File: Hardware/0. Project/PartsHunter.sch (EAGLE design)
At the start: 54 parts, among them CN1 2.1MMJACKTHM, IC1 PCF8574P, IC2 LM1117-3.3, Q1 16 MHz, U1 ATMEGA328P-AU

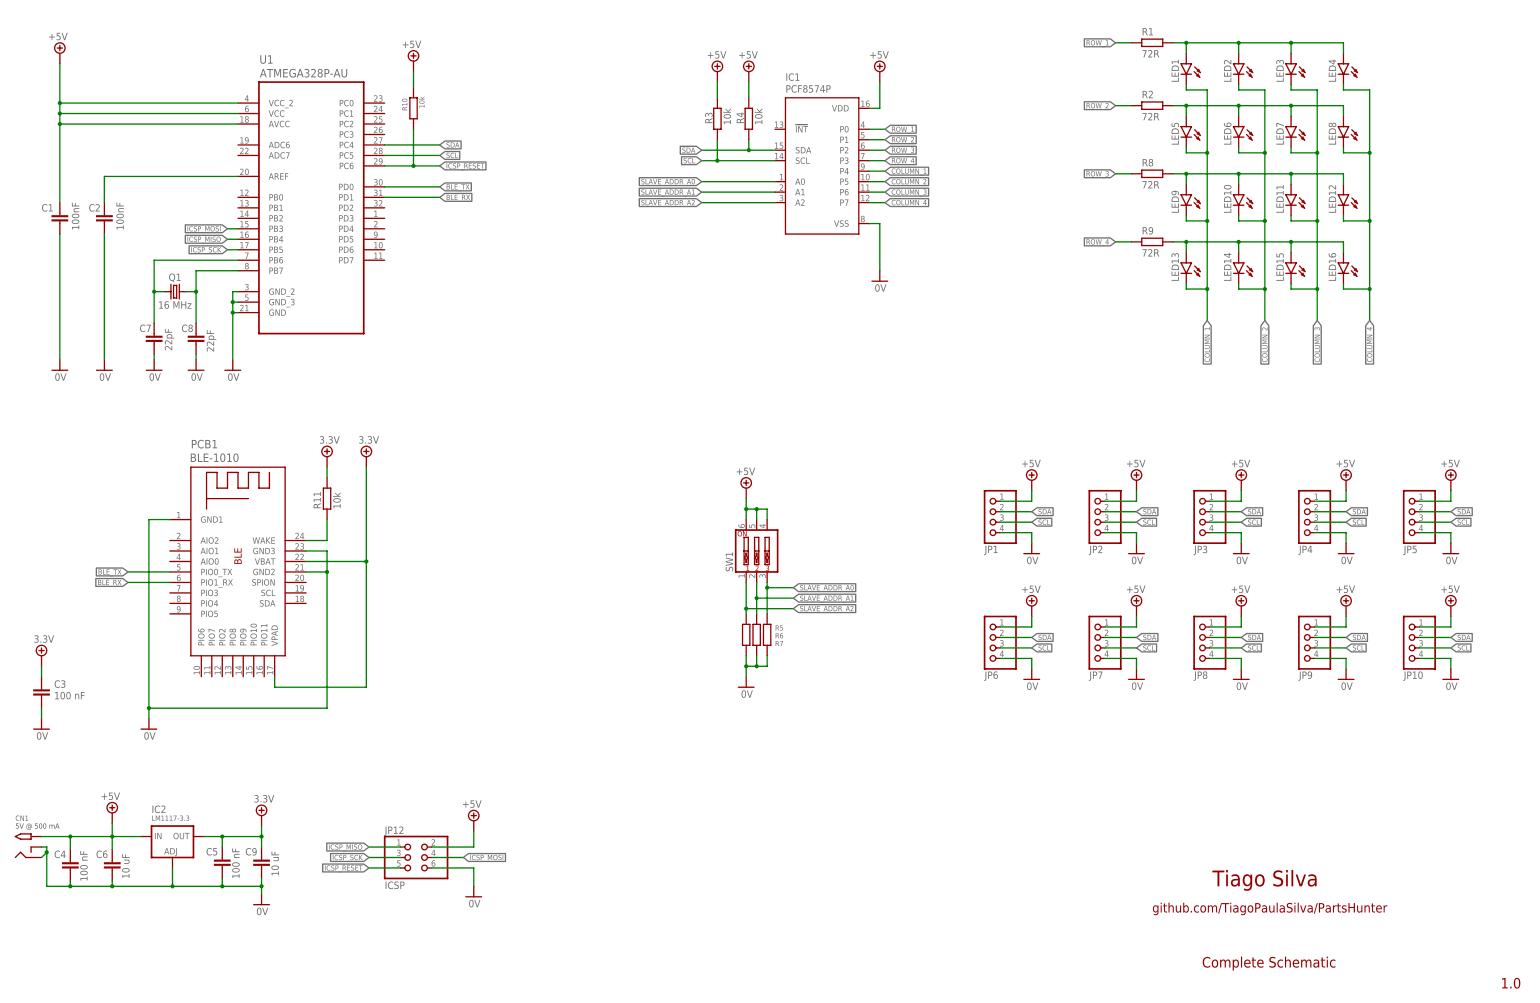
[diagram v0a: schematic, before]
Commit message: I2C pull-ups moved to master's circuit area
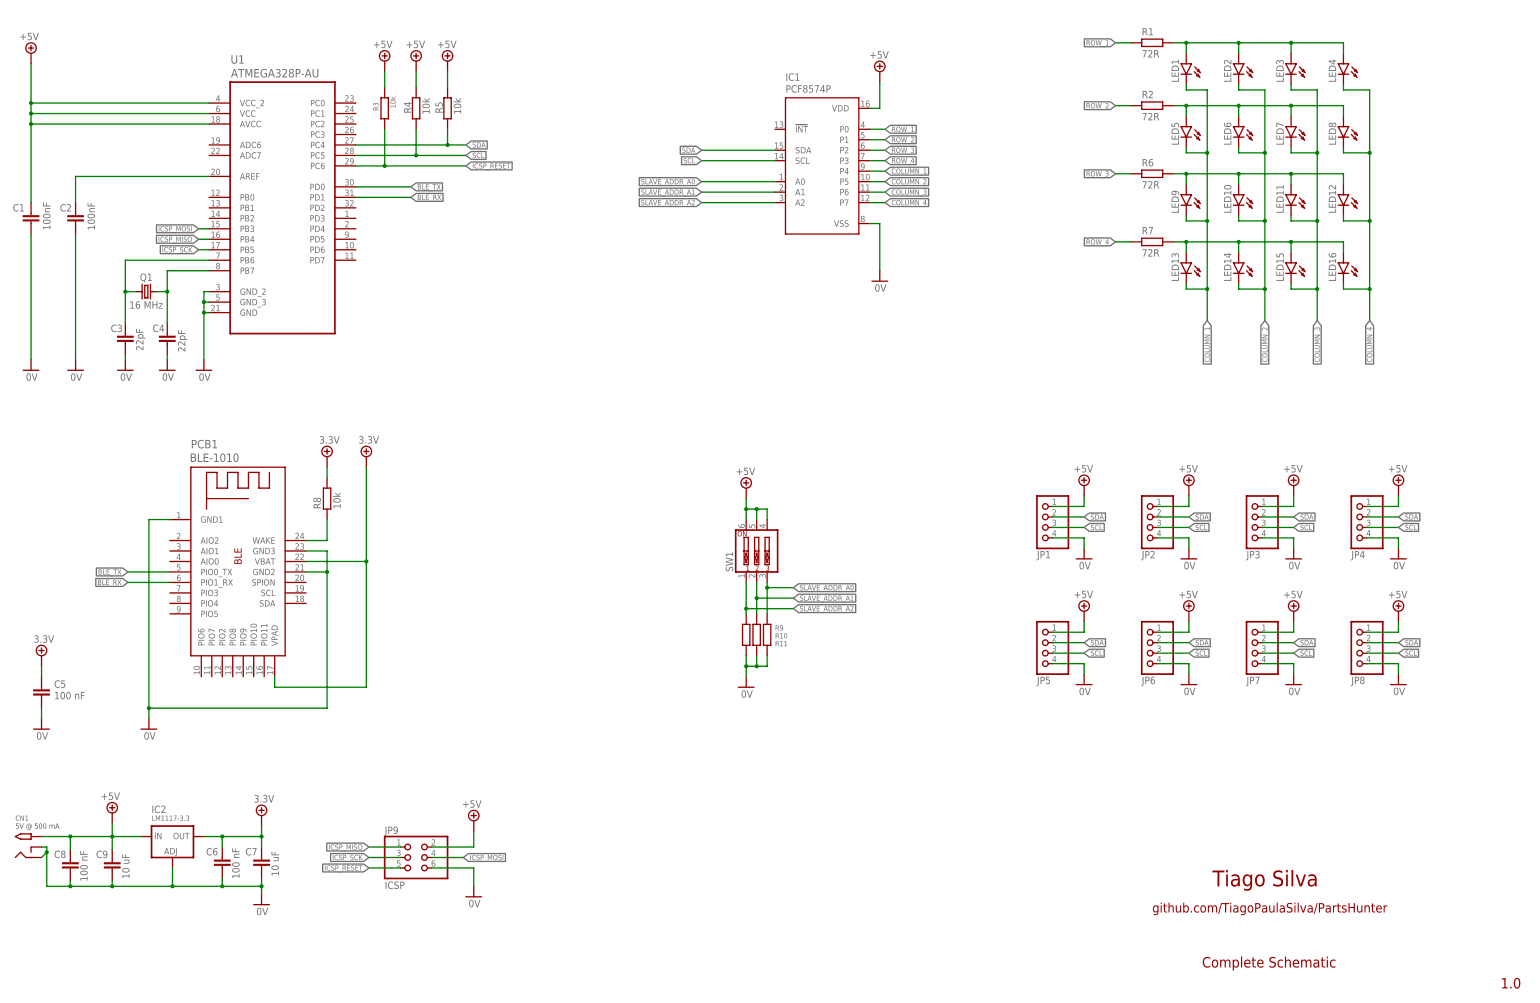
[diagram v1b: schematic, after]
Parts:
- removed JP10: (no value), pinhead:PINHD-1X4
- removed JP12: ICSP, pinhead:PINHD-2X3
- C3, C4: value 100 nF -> 22pF
- C6: value 10 uF -> 100 nF
- C7: value 22pF -> 10 uF
- C8: value 22pF -> 100 nF
- JP5: device pinhead:PINHD-1X4 -> pinhead:PINHD-1X4/90
- JP9: value (none) -> ICSP; device pinhead:PINHD-1X4/90 -> pinhead:PINHD-2X3
- R11: device rcl:R-EU_R0603 -> rcl:R-EU_R0805
- R6, R7: value 10k -> 72R
- R8: value 72R -> 10k; device rcl:R-EU_R0805 -> rcl:R-EU_R0603
- R9: value 72R -> 10k
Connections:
- net +5V: now also C8.1, C9.1, JP9.2, R5.1; no longer C4.1, C6.1, JP10.1, JP12.2, JP9.1, R10.1
- net 0V: now also C3.1, C4.1, C7.2, C8.2, JP9.6, R10.2, R11.2, R9.2; no longer C3.2, C4.2, C7.1, C8.1, JP10.4, JP12.6, JP9.4, R5.2, R6.2, R7.2
- net 3.3V: now also C6.1, C7.1, R8.1; no longer C3.1, C9.1, R11.1
- net BLE_WAKE: now also R8.2; no longer R11.2
- net ICSP_MISO: now also JP9.1; no longer JP12.1
- net ICSP_MOSI: now also JP9.4; no longer JP12.4
- net ICSP_RESET: now also JP9.5, R3.2; no longer JP12.5, R10.2
- net ICSP_SCK: now also JP9.3; no longer JP12.3
- net N$1: now also C3.2; no longer C7.2
- net N$2: now also C4.2; no longer C8.2
- net N$7: now also R6.1; no longer R8.1
- net N$8: now also R7.1; no longer R9.1
- net ROW_3: now also R6.2; no longer R8.2
- net ROW_4: now also R7.2; no longer R9.2
- net SCL: now also R4.2; no longer JP10.3, JP9.3, R3.2
- net SDA: now also R5.2; no longer JP10.2, JP9.2, R4.2
- net SLAVE_ADDR_A0: now also R11.1; no longer R7.1
- net SLAVE_ADDR_A1: now also R10.1; no longer R6.1
- net SLAVE_ADDR_A2: now also R9.1; no longer R5.1
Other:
- moved on the sheet: C1, C2, C3, C4, C5, C6, C7, C8, C9, JP1, JP2, JP3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

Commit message: SMD and PTH led option added
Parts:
- LED1, LED10, LED11, LED12, LED13, LED14, LED15, LED16, LED2, LED3, LED4, LED5, LED6, LED7, LED8, LED9: device led:LEDKA-3528ASYC -> led2:LEDKA-3528ASYC
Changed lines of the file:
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@@
 <parts>
 <part name="IC1" library="micro-philips" library_urn="urn:adsk.eagle:library:290" deviceset="PCF8574" device="P" package3d_urn="urn:adsk.eagle:package:20171/1"/>
-<part name="LED4" library="led" library_urn="urn:adsk.eagle:library:259" deviceset="LED" device="KA-3528ASYC" package3d_urn="urn:adsk.eagle:package:15831/1"/>
-<part name="LED3" library="led" library_urn="urn:adsk.eagle:library:259" deviceset="LED" device="KA-3528ASYC" package3d_urn="urn:adsk.eagle:package:15831/1"/>
-<part name="LED2" library="led" library_urn="urn:adsk.eagle:library:259" deviceset="LED" device="KA-3528ASYC" package3d_urn="urn:adsk.eagle:package:15831/1"/>
-<part name="LED1" library="led" library_urn="urn:adsk.eagle:library:259" deviceset="LED" device="KA-3528ASYC" package3d_urn="urn:adsk.eagle:package:15831/1"/>
-<part name="LED8" library="led" library_urn="urn:adsk.eagle:library:259" deviceset="LED" device="KA-3528ASYC" package3d_urn="urn:adsk.eagle:package:15831/1"/>
-<part name="LED7" library="led" library_urn="urn:adsk.eagle:library:259" deviceset="LED" device="KA-3528ASYC" package3d_urn="urn:adsk.eagle:package:15831/1"/>
-<part name="LED6" library="led" library_urn="urn:adsk.eagle:library:259" deviceset="LED" device="KA-3528ASYC" package3d_urn="urn:adsk.eagle:package:15831/1"/>
-<part name="LED5" library="led" library_urn="urn:adsk.eagle:library:259" deviceset="LED" device="KA-3528ASYC" package3d_urn="urn:adsk.eagle:package:15831/1"/>
-<part name="LED12" library="led" library_urn="urn:adsk.eagle:library:259" deviceset="LED" device="KA-3528ASYC" package3d_urn="urn:adsk.eagle:package:15831/1"/>
-<part name="LED11" library="led" library_urn="urn:adsk.eagle:library:259" deviceset="LED" device="KA-3528ASYC" package3d_urn="urn:adsk.eagle:package:15831/1"/>
-<part name="LED10" library="led" library_urn="urn:adsk.eagle:library:259" deviceset="LED" device="KA-3528ASYC" package3d_urn="urn:adsk.eagle:package:15831/1"/>
-<part name="LED9" library="led" library_urn="urn:adsk.eagle:library:259" deviceset="LED" device="KA-3528ASYC" package3d_urn="urn:adsk.eagle:package:15831/1"/>
-<part name="LED16" library="led" library_urn="urn:adsk.eagle:library:259" deviceset="LED" device="KA-3528ASYC" package3d_urn="urn:adsk.eagle:package:15831/1"/>
-<part name="LED15" library="led" library_urn="urn:adsk.eagle:library:259" deviceset="LED" device="KA-3528ASYC" package3d_urn="urn:adsk.eagle:package:15831/1"/>
-<part name="LED14" library="led" library_urn="urn:adsk.eagle:library:259" deviceset="LED" device="KA-3528ASYC" package3d_urn="urn:adsk.eagle:package:15831/1"/>
-<part name="LED13" library="led" library_urn="urn:adsk.eagle:library:259" deviceset="LED" device="KA-3528ASYC" package3d_urn="urn:adsk.eagle:package:15831/1"/>
+<part name="LED4" library="led2" deviceset="LED" device="KA-3528ASYC" package3d_urn="urn:adsk.eagle:package:15831/1"/>
+<part name="LED3" library="led2" deviceset="LED" device="KA-3528ASYC" package3d_urn="urn:adsk.eagle:package:15831/1"/>
+<part name="LED2" library="led2" deviceset="LED" device="KA-3528ASYC" package3d_urn="urn:adsk.eagle:package:15831/1"/>
+<part name="LED1" library="led2" deviceset="LED" device="KA-3528ASYC" package3d_urn="urn:adsk.eagle:package:15831/1"/>
+<part name="LED8" library="led2" deviceset="LED" device="KA-3528ASYC" package3d_urn="urn:adsk.eagle:package:15831/1"/>
+<part name="LED7" library="led2" deviceset="LED" device="KA-3528ASYC" package3d_urn="urn:adsk.eagle:package:15831/1"/>
+<part name="LED6" library="led2" deviceset="LED" device="KA-3528ASYC" package3d_urn="urn:adsk.eagle:package:15831/1"/>
+<part name="LED5" library="led2" deviceset="LED" device="KA-3528ASYC" package3d_urn="urn:adsk.eagle:package:15831/1"/>
+<part name="LED12" library="led2" deviceset="LED" device="KA-3528ASYC" package3d_urn="urn:adsk.eagle:package:15831/1"/>
+<part name="LED11" library="led2" deviceset="LED" device="KA-3528ASYC" package3d_urn="urn:adsk.eagle:package:15831/1"/>
+<part name="LED10" library="led2" deviceset="LED" device="KA-3528ASYC" package3d_urn="urn:adsk.eagle:package:15831/1"/>
+<part name="LED9" library="led2" deviceset="LED" device="KA-3528ASYC" package3d_urn="urn:adsk.eagle:package:15831/1"/>
+<part name="LED16" library="led2" deviceset="LED" device="KA-3528ASYC" package3d_urn="urn:adsk.eagle:package:15831/1"/>
+<part name="LED15" library="led2" deviceset="LED" device="KA-3528ASYC" package3d_urn="urn:adsk.eagle:package:15831/1"/>
+<part name="LED14" library="led2" deviceset="LED" device="KA-3528ASYC" package3d_urn="urn:adsk.eagle:package:15831/1"/>
+<part name="LED13" library="led2" deviceset="LED" device="KA-3528ASYC" package3d_urn="urn:adsk.eagle:package:15831/1"/>
 <part name="R1" library="rcl" library_urn="urn:adsk.eagle:library:334" deviceset="R-EU_" device="R0805" package3d_urn="urn:adsk.eagle:package:23553/2" value="72R"/>
 <part name="R2" library="rcl" library_urn="urn:adsk.eagle:library:334" deviceset="R-EU_" device="R0805" package3d_urn="urn:adsk.eagle:package:23553/2" value="72R"/>

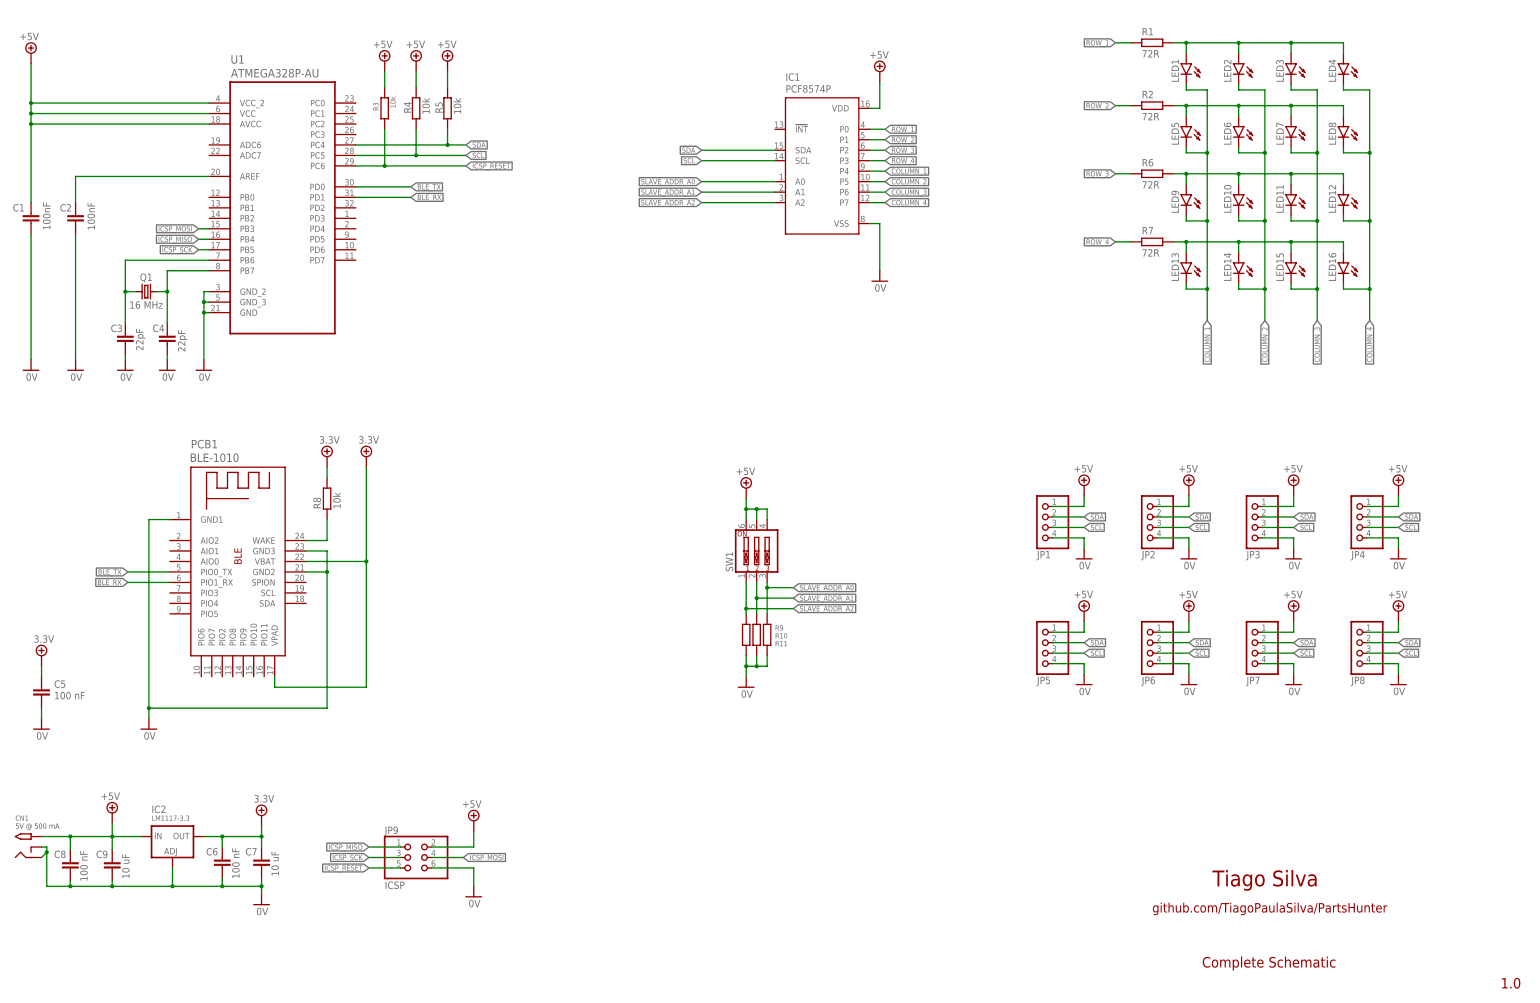
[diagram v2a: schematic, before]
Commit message: Working on 2.0 PCB (bug fix)
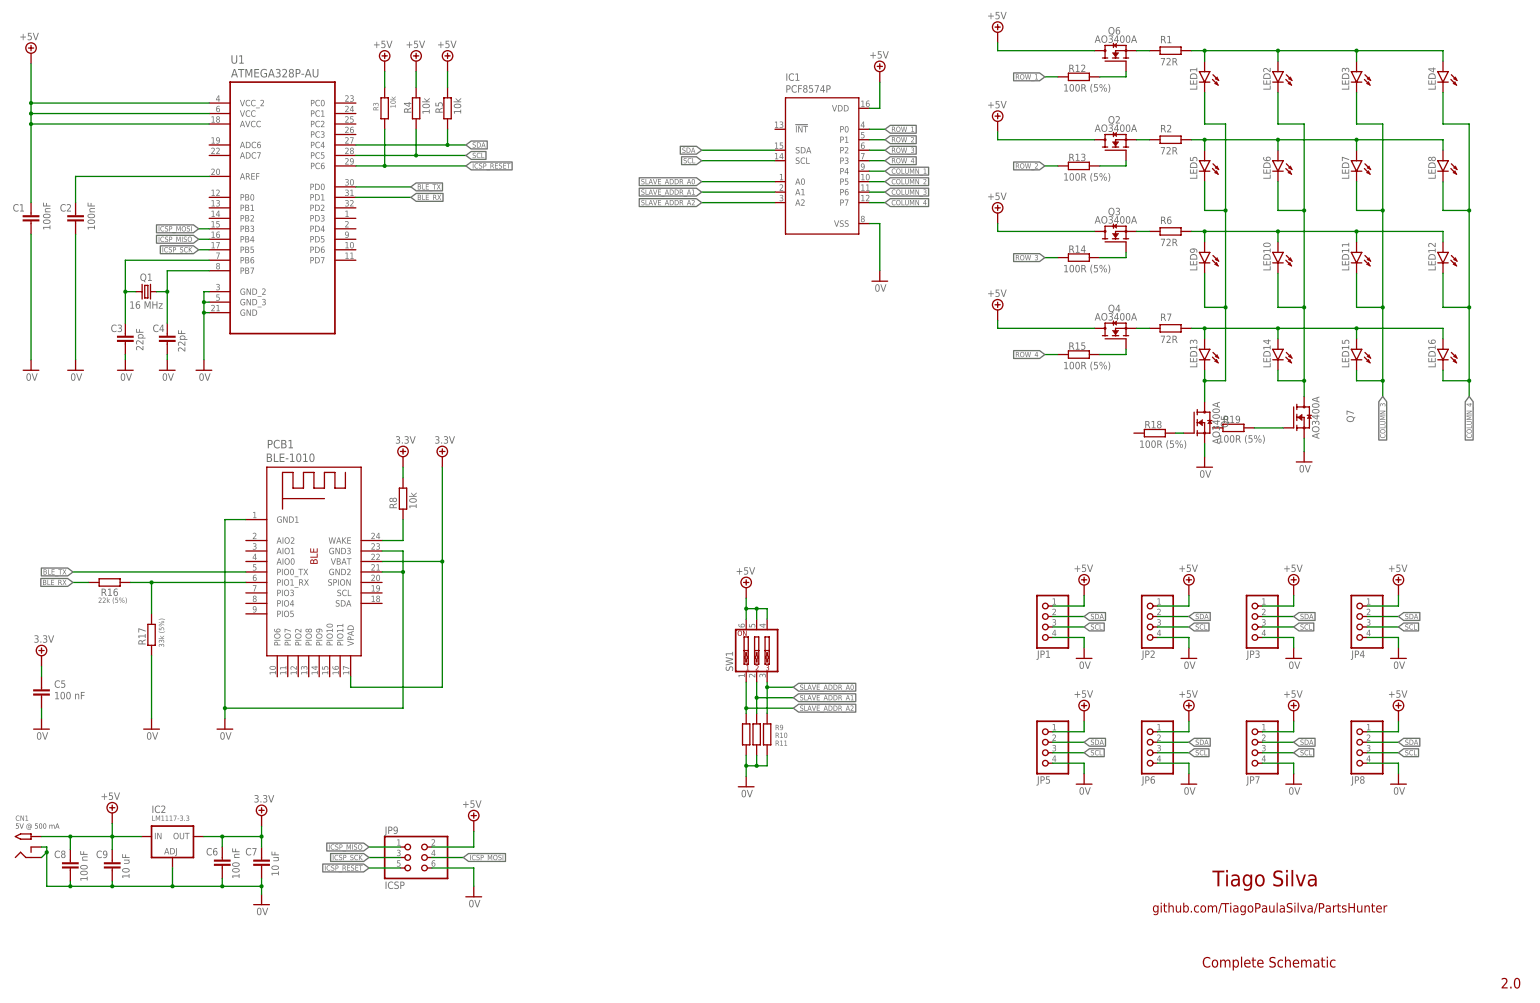
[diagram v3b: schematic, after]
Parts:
- added Q2, Q3, Q4, Q5, Q6, Q7: AO3400A, AO3400A:AO3400A
- added R12, R13, R14, R15, R18, R19: 100R (5%), rcl:R-EU_R0805
- added R16: 22k (5%), rcl:R-EU_R0805
- added R17: 33k (5%), rcl:R-EU_R0805
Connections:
- new net N$10: Q2.S, R2.2
- new net N$11: Q3.G, R14.2
- new net N$12: Q3.S, R6.2
- new net N$13: Q2.G, R13.2
- new net N$14: Q4.S, R7.2
- new net N$15: PCB1.PIO1_RX, R16.2, R17.2
- new net N$16: Q5.G, R18.2
- new net N$18: Q7.G, R19.2
- new net N$3: Q6.G, R12.2
- new net N$4: Q6.S, R1.2
- new net N$9: Q4.G, R15.2
- net +5V: now also Q2.D, Q3.D, Q4.D, Q6.D
- net 0V: now also Q5.S, Q7.S, R17.1
- net BLE_RX: now also R16.1; no longer PCB1.PIO1_RX
- net COLUMN_1: now also Q5.D
- net COLUMN_2: now also Q7.D
- net ROW_1: now also R12.1; no longer R1.2
- net ROW_2: now also R13.1; no longer R2.2
- net ROW_3: now also R14.1; no longer R6.2
- net ROW_4: now also R15.1; no longer R7.2
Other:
- note added: "2.0"
- note removed: "1.0"
- moved on the sheet: JP1, JP2, JP3, JP4, JP5, JP6, JP7, JP8, LED1, LED10, LED11, LED12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
